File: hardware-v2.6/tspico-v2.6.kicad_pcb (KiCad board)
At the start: 4 copper layers, 130 x 56 mm, 100 parts, among them J1 USB-C, P1 TS2068_Edge, P10 Flash WE, Q1 MMBT3904, SW1 NMI, SW2 TS Reset, SW3 Pico Reset, SW4 BOOTSEL, U1 74LS04, U10 SST39SF040-70-4C-PHE, U11 NE555, U13 AS6C4008-55PCN, U2 RP2040, U21 W25Q16JVSSIQ, U22 AMS1117-3.3, U3 microSD, U4 74LS32, U5 74LS27, U6 74LVC245APW, U7 74LVC245APW, U8 74LS157, U9 74LS09, Y1 12MHz

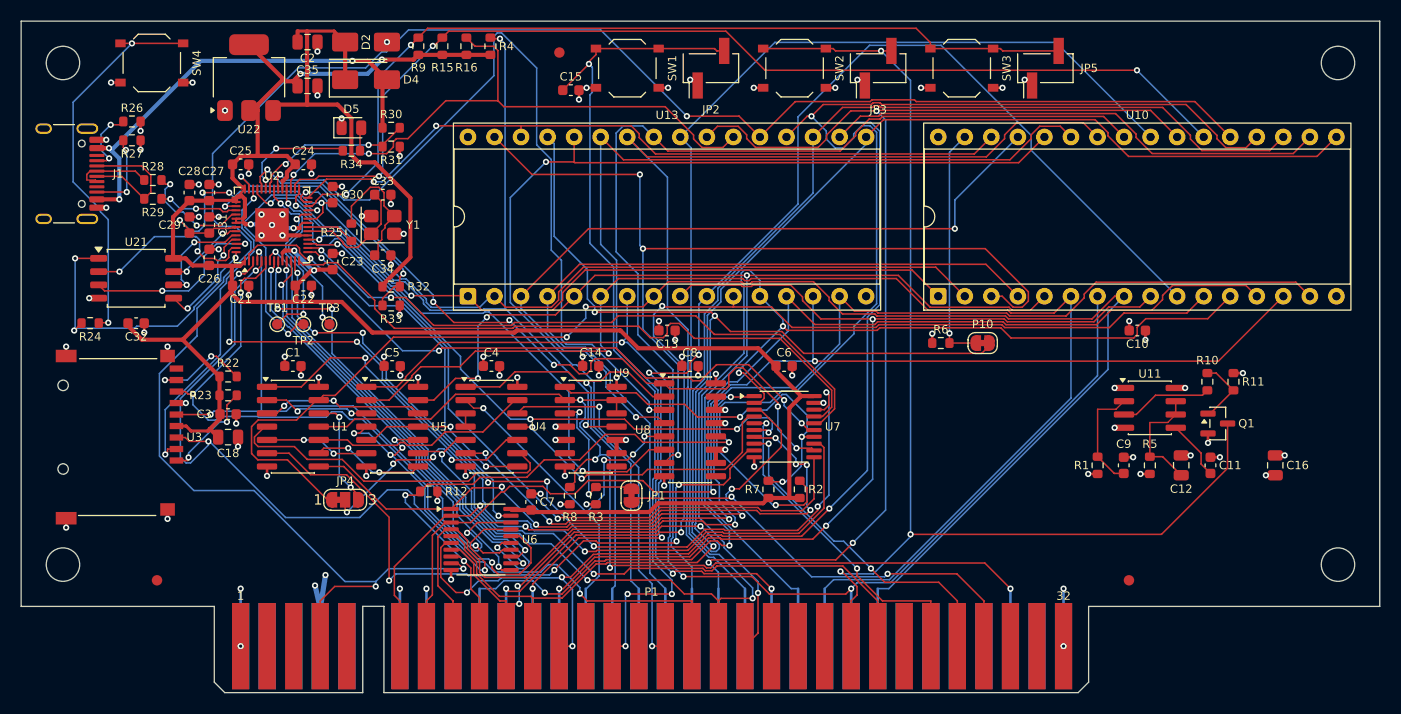
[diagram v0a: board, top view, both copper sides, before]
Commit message: v2.6 prototype 2: glue logic in 74LVC, TPS3808 reset
The v2.2 glue (74LS04/27/32/09/157) is rebuilt in 74LVC at 3.3 V, because
the SN74LS09 (56) and XL74LS27 (108) were scarce at JLCPCB and every glue
output already ends at a 3.3 V part. Same logic at every Pico pin, so no
firmware change:

- U5 74LVC138 decodes the port (A4-A6 select; /IORQ, A7, /M1 enables);
  JP4 now picks output O0 ($00-$0F) or O1 ($10-$1F)
- U4 74LVC32: /+RW (buffered so it keeps step with /+W), /+W = /+RW-select
  OR /RD, /RDROM = A14 + A15 + /RD
- U1 74LVC1G97 (mux wired as OR with one inverted input): /MREQ_G
- U9 74LVC2G07 open-drain /BE driver; U7 channel 5 now carries /BE_IN as
  /BE_STAT, so R4 and R7 go
- U8 74LVC157 for the A14/A15 mux
- U11 TPS3808G01 replaces the 555, Q1 and passives: /RESET held below
  4.09 V and for 2.7 s after (CT 470 nF)

Checked by simulating the old and new netlists gate by gate over all
229,376 legal input states, both JP4 positions: all 12 outputs agree. The
only difference is /+W when /M1, /IORQ and /RD are all low, which a Z80
never does.

Layout: the RP2040's top/bottom-row IOVDD caps stand on their own pin's
lane with locked pin-to-cap stubs; without that the router left one net
open on three attempts. Routed first time, ERC/DRC clean at every
severity. 74 assembled parts (was 81), $9.79/board at 10.

Co-Authored-By: Claude Opus 5.5 <noreply@anthropic.com>
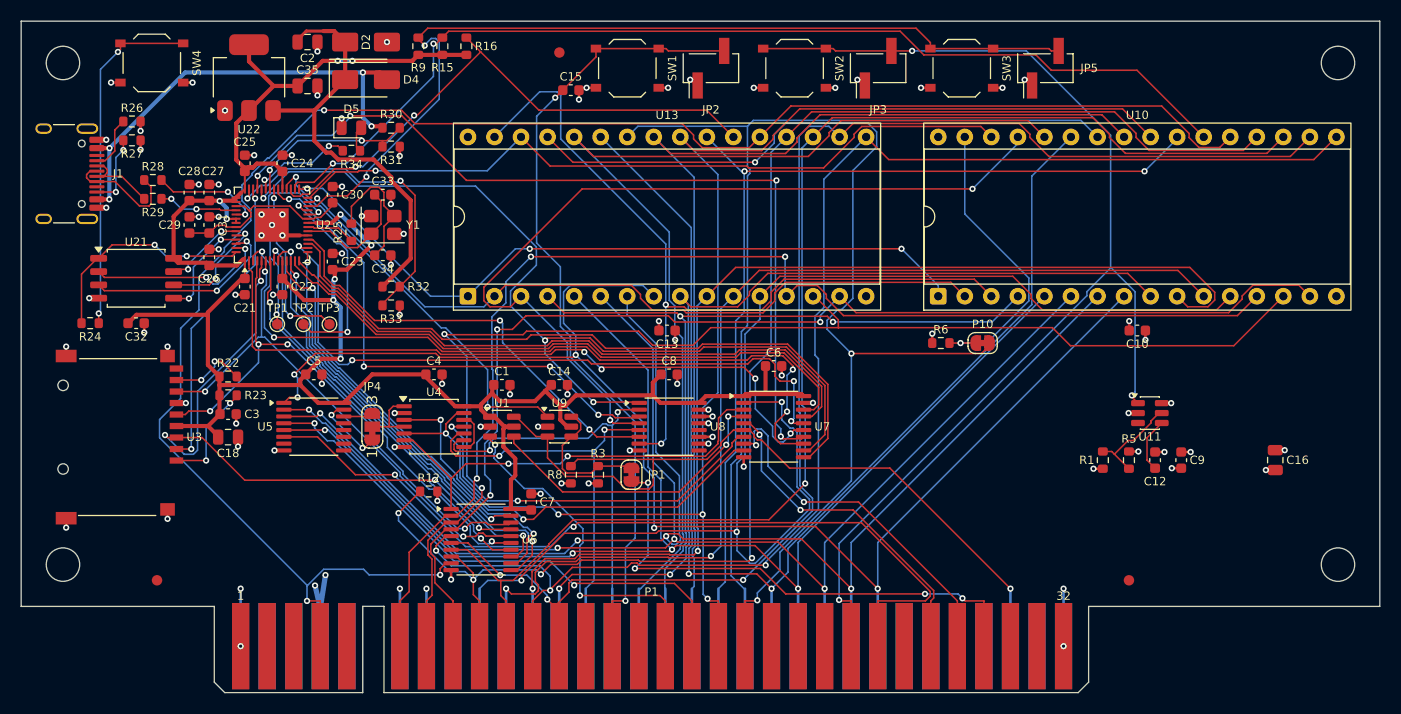
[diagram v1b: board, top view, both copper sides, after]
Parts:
- removed C11: 100n, C_0603_1608Metric
- removed Q1: MMBT3904, SOT-23
- removed R10, R2, R4, R7: 4k7, R_0603_1608Metric
- removed R11: 2k2, R_0603_1608Metric
- C12: value 10u -> 470n; footprint C_0805_2012Metric -> C_0603_1608Metric
- R1: value 1M -> 100k
- R5: value 220k -> 11k
- U1: value 74LS04 -> 74LVC1G97; footprint SOIC-14_3.9x8.7mm_P1.27mm -> SOT-23-6
- U11: value NE555 -> TPS3808G01; footprint SOIC-8_3.9x4.9mm_P1.27mm -> SOT-23-6
- U4: value 74LS32 -> 74LVC32A; footprint SOIC-14_3.9x8.7mm_P1.27mm -> TSSOP-14_4.4x5mm_P0.65mm
- U5: value 74LS27 -> 74LVC138A; footprint SOIC-14_3.9x8.7mm_P1.27mm -> TSSOP-16_4.4x5mm_P0.65mm
- U8: value 74LS157 -> 74LVC157A; footprint SOIC-16_3.9x9.9mm_P1.27mm -> TSSOP-16_4.4x5mm_P0.65mm
- U9: value 74LS09 -> 74LVC2G07; footprint SOIC-14_3.9x8.7mm_P1.27mm -> SOT-23-6
- moved C1 20.1 mm to (46.0, 34.8)
- moved U1 20.0 mm to (46.0, 38.8)
- moved C5 7.54 mm to (28.0, 33.8)
- moved U5 7.50 mm to (28.0, 38.8)
- moved JP4 7.47 mm to (33.6, 38.8), turned to 90 degrees
- moved C4 5.56 mm to (39.5, 33.8)
- moved C9 5.52 mm to (111.0, 42.0)
- moved U4 5.50 mm to (39.5, 38.8)
- moved C14 3.50 mm to (51.5, 34.8)
- moved U9 3.00 mm to (51.5, 38.8)
- moved C12 2.55 mm to (108.5, 42.0)
- moved C8 2.15 mm to (62.0, 33.8)
- moved R5 2.06 mm to (106.0, 42.0)
- moved U8 2.02 mm to (62.0, 38.8)
- moved R3 2.01 mm to (55.2, 43.4)
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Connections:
- C1 pad 1: +5V -> +3V3
- C12 pad 1: RST_TIM -> RST_CT
- C14 pad 1: +5V -> +3V3
- C4 pad 1: +5V -> +3V3
- C5 pad 1: +5V -> +3V3
- C8 pad 1: +5V -> +3V3
- C9 pad 1: RST_TRIG -> +5V
- JP4 pad 1: A4 -> DEC_00
- JP4 pad 2: PORT_A4 -> PORT_SEL
- JP4 pad 3: nA4 -> DEC_10
- R1 pad 2: RST_TRIG -> RST_SENSE
- R5 pad 1: +5V -> RST_SENSE
- R5 pad 2: RST_TIM -> GND
- U1 pad 1: nM1 -> +3V3
- U1 pad 2: M1 -> GND
- U1 pad 3: NOR567 -> nMREQ
- U1 pad 4: OR567 -> nMREQ_G
- U1 pad 5: NRW -> +3V3
- U1 pad 6: nPRW -> nBE_IN
- U11 pad 1: GND -> nRESET
- U11 pad 2: RST_TRIG -> GND
- U11 pad 3: RST_OUT -> unconnected-(U11-~{MR}-Pad3)
- U11 pad 4: +5V -> RST_CT
- U11 pad 5: RST_CONT -> RST_SENSE
- U11 pad 6: RST_TIM -> +5V
- U4 pad 1: A14 -> PORT_SEL
- U4 pad 10: PORT_A4 -> A15
- U4 pad 11: nMREQ_G -> nRDROM
- U4 pad 12: nMREQ -> A14_OR_A15
- U4 pad 13: BE_IN -> nRD
- U4 pad 14: +5V -> +3V3
- U4 pad 2: A15 -> GND
- U4 pad 3: A14_OR_A15 -> nPRW
- U4 pad 4: A14_OR_A15 -> PORT_SEL
- U4 pad 6: nRDROM -> nPW
- U4 pad 8: PX -> A14_OR_A15
- U4 pad 9: OR567 -> A14
- U5 pad 1: A5 -> A4
- U5 pad 10: nIORQ -> unconnected-(U5-O5-Pad10)
- U5 pad 11: PX -> unconnected-(U5-O4-Pad11)
- U5 pad 12: NOR567 -> unconnected-(U5-O3-Pad12)
- U5 pad 13: A7 -> unconnected-(U5-O2-Pad13)
- U5 pad 14: +5V -> DEC_10
- U5 pad 2: A6 -> A5
- U5 pad 3: M1 -> A6
- U5 pad 5: PX -> A7
- U5 pad 6: NRW -> nM1
- U5 pad 7: GND -> unconnected-(U5-O7-Pad7)
- U5 pad 8: NW -> GND
- U5 pad 9: nRD -> unconnected-(U5-O6-Pad9)
- U7 pad 1: U7_DIR -> +3V3
- U7 pad 14: BE_L_BUF -> nBE_STAT
- U7 pad 6: nBE_L -> nBE_IN
- U8 pad 16: +5V -> +3V3
- U9 pad 1: BE_L_BUF -> nBE_L
- U9 pad 2: nBE_IN -> GND
- U9 pad 3: nBE_DRV -> nBE_IN
- U9 pad 4: GND -> nBE_DRV
- U9 pad 5: GND -> +3V3
- U9 pad 6: unconnected-(U9-Pad6) -> nBE_DRV
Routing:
- net BE_L_BUF: track 36.2 -> 0.00 mm, vias 3 -> 0
- net OR567: track 32.8 -> 0.00 mm
- net A14_B: track 77.3 -> 49.8 mm, vias 2 -> 4
- net nBE_L: track 62.4 -> 37.8 mm, vias 4 -> 2
- net nBE_IN: track 99.3 -> 75.5 mm, vias 4 -> 1
- net A0_L: track 83.1 -> 59.4 mm, vias 8 -> 0
- net nPRW: track 64.3 -> 41.6 mm, vias 4 -> 2
- net PORT_A4: track 21.8 -> 0.00 mm, vias 4 -> 0
- net U7_DIR: track 21.3 -> 0.00 mm, vias 2 -> 0
- net BE_IN: track 21.2 -> 0.00 mm
- net A10: track 115.2 -> 94.3 mm, vias 3 -> 2
- net nROSCS_L: track 71.6 -> 91.2 mm, vias 6 -> 3
- net nPW: track 60.3 -> 41.1 mm, vias 4 -> 2
- net D7: track 191.0 -> 173.9 mm
- net PX: track 16.8 -> 0.00 mm, vias 2 -> 0
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
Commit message: CERN-OHL-S-2.0 licence; board labels and OSHW logo on v3 and v2.6
- LICENSE: CERN Open Hardware Licence v2, Strongly Reciprocal, for the
  hardware designs; the README says what it covers and what it does not
  (firmware/, the Pico SDK import file, Zimodem, KiCad library parts).
- hardware/scripts/labels.py: board name on the top silkscreen; name,
  repository URL (the licence's Source Location), licence and the OSHW logo
  on the bottom. Silkscreen only, rerunnable on a routed board, and it
  refuses to save a label that lands on a pad, courtyard or other silk.
  Both flow.py scripts run it last, since gen_layout.py rebuilds the board.
- Applied to the v3 and v2.6 boards: copper untouched, DRC clean at every
  severity. v3 PCB PDF and both boards' renders regenerated.

Not tagged: the labels go into each board's next revision.

Co-Authored-By: Claude Opus 5.5 <noreply@anthropic.com>
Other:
- board text added: "CERN-OHL-S-2.0"
- board text added: "TS-Pico v2.6"
- board text added: "github.com/factus10/tspico-hardware"
